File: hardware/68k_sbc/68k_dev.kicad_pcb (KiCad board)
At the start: 2 copper layers, 186.7 x 144.8 mm, 71 parts, among them IC1 DS1813-10+T&R, J1 640456-3, J2 Passive_Bus_ISA_16bit, J3 Conn_02x20_Odd_Even, J4 JTAG, J5 Barrel_Jack, SW1 SW_DPST_x2, U1 68000D, U10 CY7C1049D, U11 CY7C1049D, U12 CY7C1049D, U13 CY7C1049D, U14 16550, U15 TXS0108EPW, U2 M27C1024, U3 EPM7128SLC84-15N, U5 AMS1117-3.3, U6 CY7C1049D, U7 CY7C1049D, U8 CY7C1049D, U9 CY7C1049D, X1 CXO_DIP8, X2 CXO_DIP14

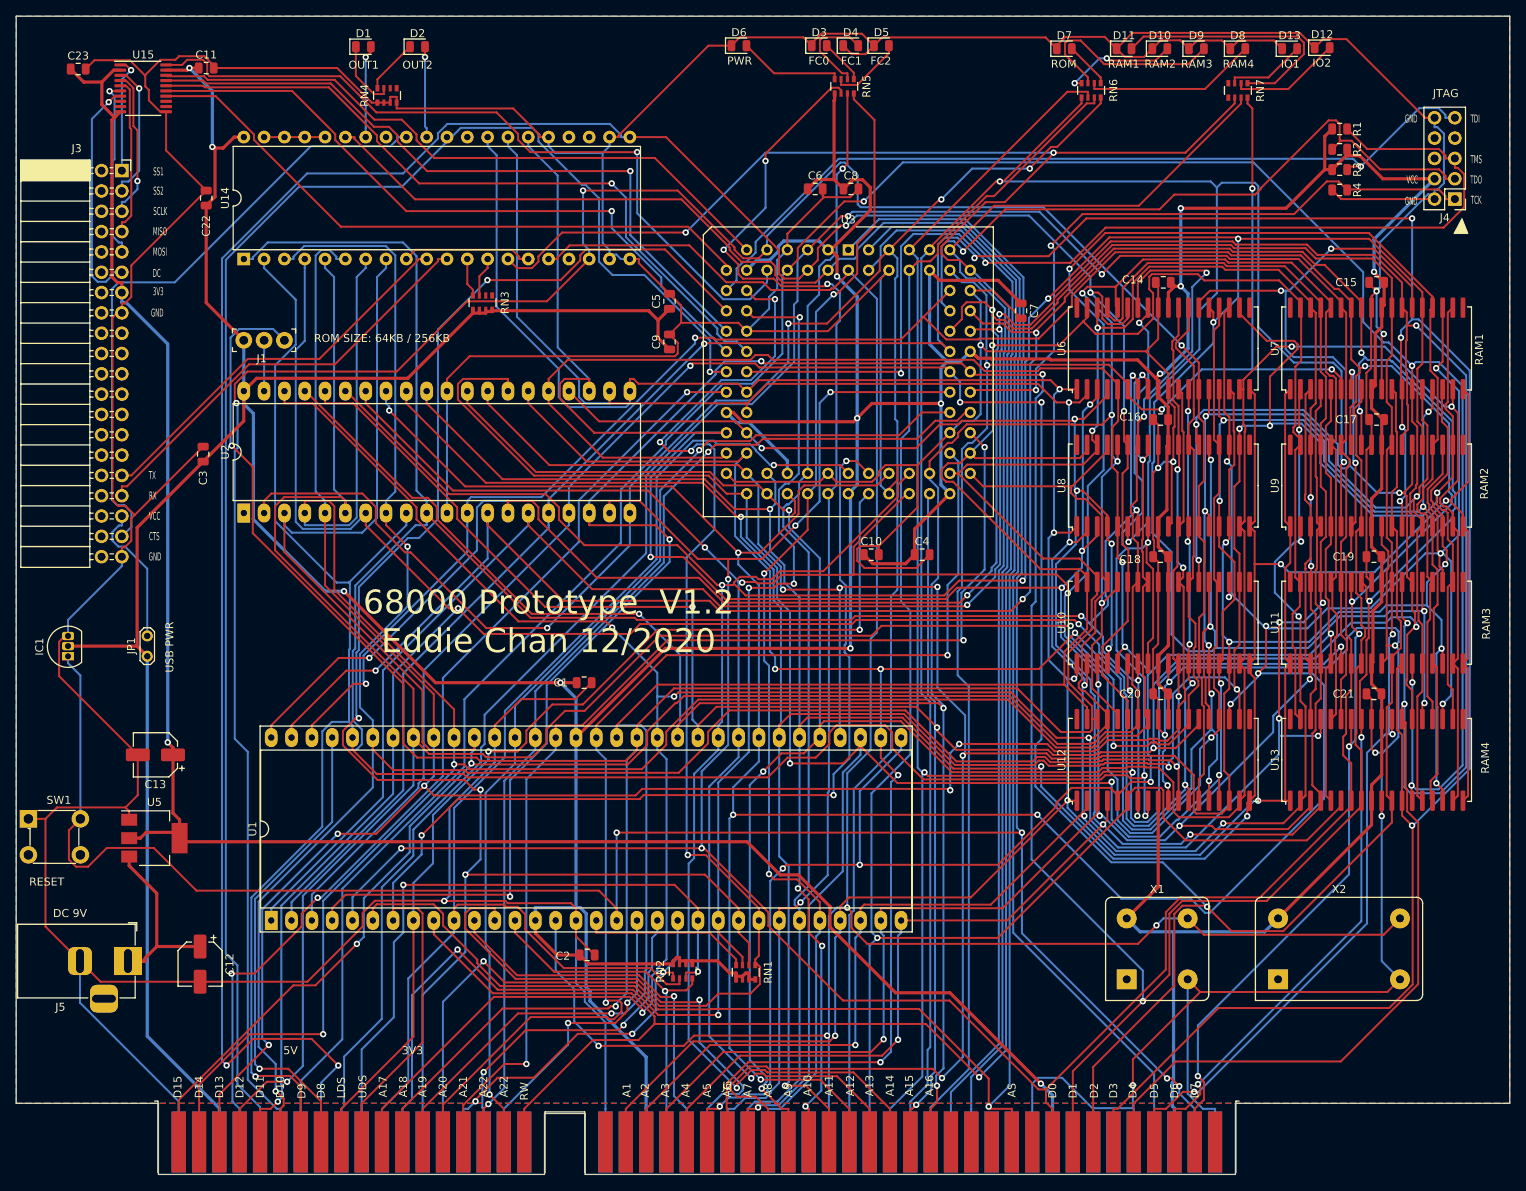
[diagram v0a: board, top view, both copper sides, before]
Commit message: Fixed v1.2 pcb design bug
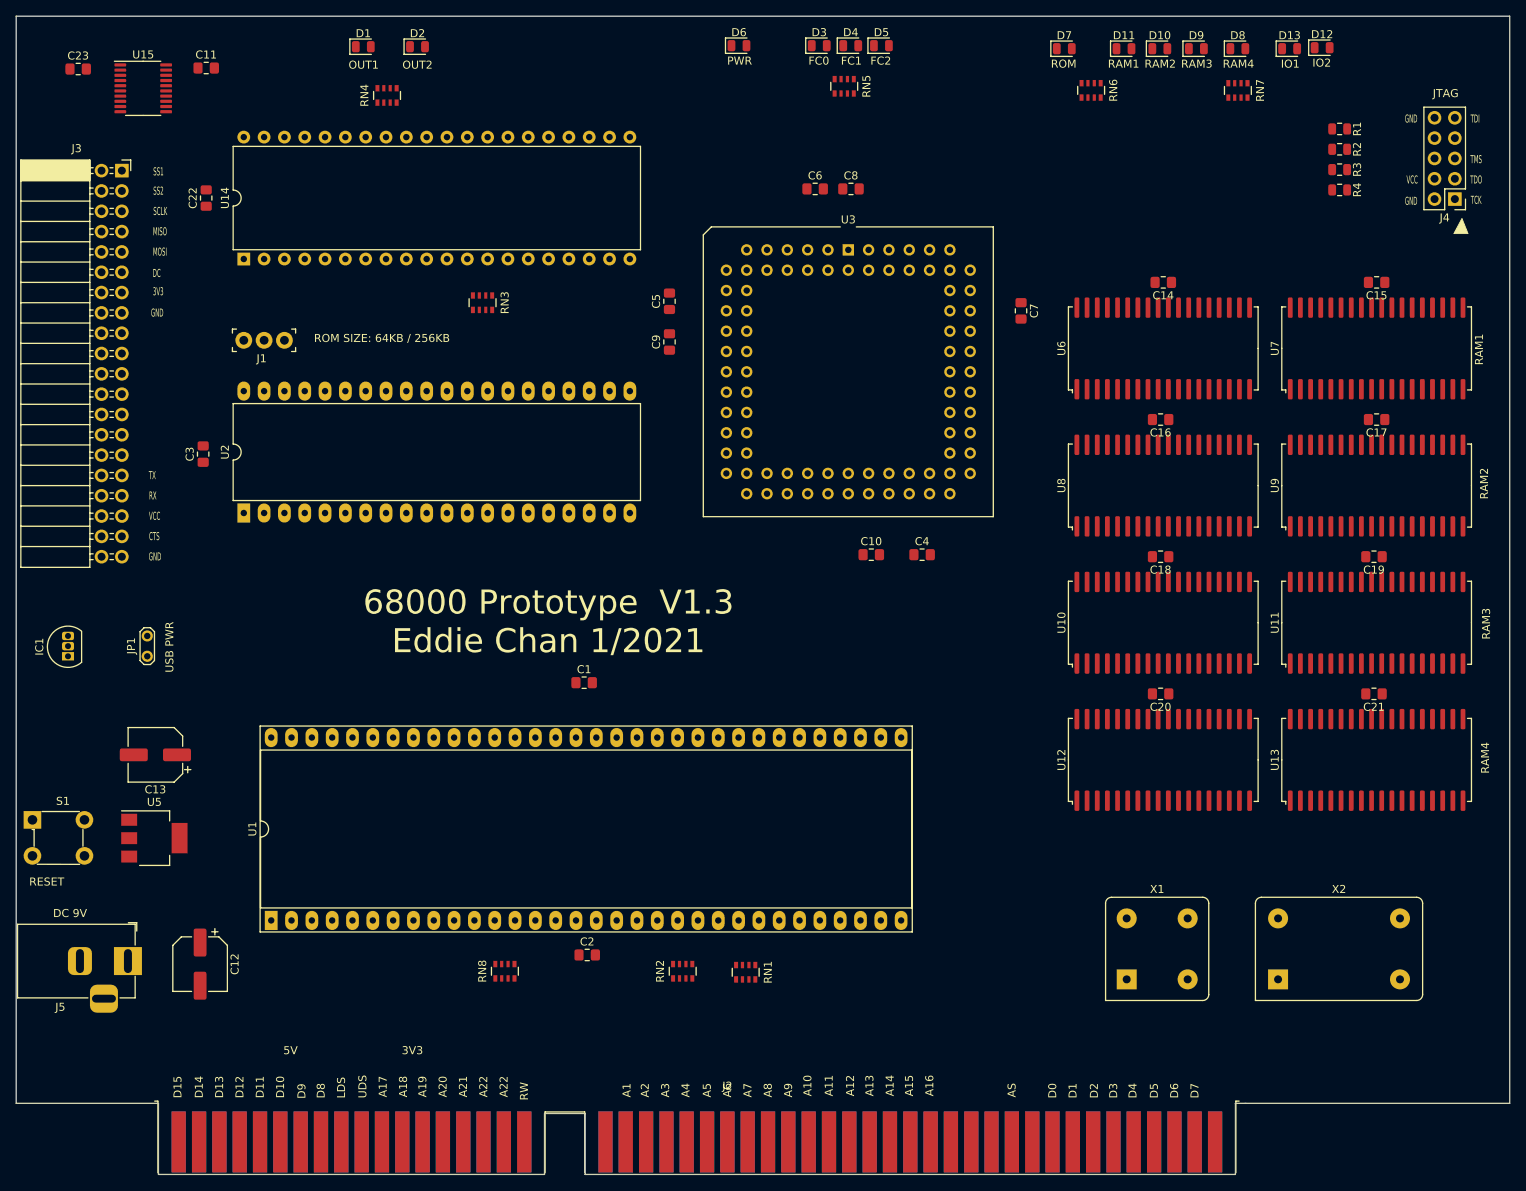
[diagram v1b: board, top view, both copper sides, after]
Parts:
- removed SW1: SW_DPST_x2, digikey-footprints:Switch_Tactile_THT_6x6mm
- added RN8: 470, Resistor_SMD:R_Array_Convex_4x0603, F.Cu at (77.6, 133.3)
- added S1: 1825910-6, digikey-footprints:Switch_Tactile_THT_6x6mm, F.Cu at (18.5, 114.4)
- C1, C10, C11, C14, C15, C16, C17, C18, C19, C2, C20, C21, C22, C23, C3, C4, C5, C6, C7, C8, C9: footprint Capacitor_SMD:C_0805_2012Metric -> Capacitor_SMD:C_0805_2012Metric_Pad1.15x1.40mm_HandSolder
- C12, C13: footprint Capacitor_SMD:CP_Elec_5x5.4 -> Capacitor_SMD:CP_Elec_6.3x7.7
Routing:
- net GND: track 1224.0 -> 0.00 mm, vias 13 -> 0
- net VCC: track 968.4 -> 0.00 mm, vias 12 -> 0
- net A14: track 481.0 -> 0.00 mm, vias 10 -> 0
- net A13: track 458.3 -> 0.00 mm, vias 6 -> 0
- net A12: track 431.2 -> 0.00 mm, vias 13 -> 0
- net A15: track 428.4 -> 0.00 mm, vias 10 -> 0
- net D4: track 422.5 -> 0.00 mm, vias 6 -> 0
- net A17: track 410.1 -> 0.00 mm, vias 8 -> 0
- net A18: track 404.0 -> 0.00 mm, vias 6 -> 0
- net D3: track 400.2 -> 0.00 mm, vias 7 -> 0
- net A3: track 382.8 -> 0.00 mm, vias 9 -> 0
- net A16: track 376.5 -> 0.00 mm, vias 7 -> 0
- net A8: track 372.5 -> 0.00 mm, vias 10 -> 0
- net A6: track 367.6 -> 0.00 mm, vias 11 -> 0
- net A11: track 363.1 -> 0.00 mm, vias 7 -> 0
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- removed copper zone on B.Cu, net GND
- removed copper zone on F.Cu, net GND
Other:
- board text added: "68000 Prototype V1.3 Eddie Chan 1/2021"
- board text removed: "68000 Prototype V1.2 Eddie Chan 12/2020"

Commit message: lib refactor
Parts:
- removed D10, D11, D12, D13, D8, D9: LED, LED_SMD:LED_0805_2012Metric
- removed RN6, RN7: 470, Resistor_SMD:R_Array_Convex_4x0603
- added C24: 100nF, Capacitor_SMD:C_0805_2012Metric_Pad1.15x1.40mm_HandSolder, B.Cu at (153.5, 72.8)
- added C25: 100nF, Capacitor_SMD:C_0805_2012Metric_Pad1.15x1.40mm_HandSolder, B.Cu at (153.5, 89.9)
- added C26: 100nF, Capacitor_SMD:C_0805_2012Metric_Pad1.15x1.40mm_HandSolder, B.Cu at (153.7, 55.1)
- added C27: 100nF, Capacitor_SMD:C_0805_2012Metric_Pad1.15x1.40mm_HandSolder, B.Cu at (181.5, 72.4)
- added U16: CY7C1049D, KiCad_Libraries:SOJ-36_10.16x23.49mm_P1.27mm_sram, F.Cu at (153.6, 55.3)
- added U17: CY7C1049D, KiCad_Libraries:SOJ-36_10.16x23.49mm_P1.27mm_sram, F.Cu at (181.5, 72.6)
- added U18: CY7C1049D, KiCad_Libraries:SOJ-36_10.16x23.49mm_P1.27mm_sram, F.Cu at (153.5, 72.6)
- added U4: CY7C1049D, KiCad_Libraries:SOJ-36_10.16x23.49mm_P1.27mm_sram, F.Cu at (181.6, 55.3)
- C1, C10, C11, C14, C15, C16, C17, C18, C19, C2, C20, C21, C22, C23, C3, C4, C5, C6, C7, C8, C9, RN2, RN8: moved to B.Cu
- moved C3 112.6 mm to (144.7, 27.6), turned to 270 degrees
- moved U2 106.6 mm to (144.7, 38.2)
- moved J1 94.8 mm to (137.9, 19.1)
- moved U7 92.2 mm to (153.5, 141.5), turned to 270 degrees
- moved U6 88.7 mm to (181.5, 141.5), turned to 270 degrees
- moved C16 77.7 mm to (153.5, 141.9), turned to 0 degrees
- moved C17 77.1 mm to (181.5, 141.4), turned to 0 degrees
- moved J4 74.5 mm to (124.0, 19.2), turned to 270 degrees
- moved D7 74.5 mm to (73.0, 18.7)
- moved R1 66.9 mm to (115.1, 29.8), turned to 90 degrees
- moved R2 64.3 mm to (117.6, 29.8), turned to 270 degrees
- moved R3 61.9 mm to (120.1, 29.8), turned to 90 degrees
- moved U9 61.3 mm to (153.5, 124.3), turned to 270 degrees
- moved X2 60.1 mm to (114.7, 142.6)
- moved R4 59.6 mm to (122.7, 29.8), turned to 270 degrees
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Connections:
- D7 pad 1: GND -> Net-(D7-Pad1)
- D7 pad 2: Net-(D7-Pad2) -> VCC
- J2 pad 13: IO_SEL1 -> Net-(J2-Pad13)
- J2 pad 14: IO_SEL2 -> Net-(J2-Pad14)
- J2 pad 15: RAM1_SEL -> Net-(J2-Pad15)
- J2 pad 16: RAM2_SEL -> Net-(J2-Pad16)
- J2 pad 17: RAM3_SEL -> Net-(J2-Pad17)
- J2 pad 18: RAM4_SEL -> Net-(J2-Pad18)
- J2 pad 19: ROM_SEL -> Net-(J2-Pad19)
- J2 pad 4: RST_H -> Net-(J2-Pad4)
- J2 pad 72: RDL -> Net-(J2-Pad72)
- J2 pad 73: RDU -> Net-(J2-Pad73)
- J2 pad 74: WRL -> Net-(J2-Pad74)
- J2 pad 75: WRU -> Net-(J2-Pad75)
- J2 pad 76: IRQ1 -> Net-(J2-Pad76)
- J2 pad 77: IRQ2 -> Net-(J2-Pad77)
- J2 pad 9: +3V3 -> Net-(J2-Pad9)
- RN1 pad 1: IPL0 -> IPL2
- RN1 pad 3: IPL2 -> IPL0
- RN2 pad 2: DTACK -> Net-(RN2-Pad2)
- RN2 pad 4: BR -> VMA
- RN4 pad 5: Net-(RN4-Pad5) -> Net-(D7-Pad1)
- RN4 pad 7: Net-(D1-Pad1) -> Net-(D2-Pad1)
- RN4 pad 8: Net-(D2-Pad1) -> Net-(D1-Pad1)
- RN5 pad 1: Net-(D3-Pad2) -> Net-(D5-Pad2)
- RN5 pad 3: Net-(D5-Pad2) -> Net-(D3-Pad2)
- RN5 pad 5: VCC -> STATUS
- RN5 pad 6: FC2 -> FC0
- RN5 pad 8: FC0 -> FC2
- RN8 pad 1: BGACK -> Net-(RN8-Pad1)
- RN8 pad 2: VMA -> BR
- RN8 pad 3: Net-(RN8-Pad3) -> BGACK
- RN8 pad 4: Net-(RN8-Pad4) -> DTACK
- U1 pad 17: Net-(RN1-Pad4) -> Net-(RN8-Pad1)
- U14 pad 30: IRQ1 -> Net-(U14-Pad30)
- U3 pad 22: IRQ1 -> IO_SEL1
- U3 pad 24: IRQ2 -> STATUS
- U3 pad 74: IO_SEL1 -> RAM5_SEL
- U3 pad 75: IO_SEL2 -> RAM6_SEL
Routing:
- net GND: track 0.00 -> 1228.2 mm, vias 0 -> 19
- net VCC: track 0.00 -> 1070.5 mm, vias 0 -> 25
- net A3: track 0.00 -> 593.9 mm, vias 0 -> 11
- net A17: track 0.00 -> 536.0 mm, vias 0 -> 8
- net A1: track 0.00 -> 525.3 mm, vias 0 -> 5
- net A16: track 0.00 -> 472.6 mm, vias 0 -> 9
- net A7: track 0.00 -> 471.9 mm, vias 0 -> 8
- net A2: track 0.00 -> 469.3 mm, vias 0 -> 10
- net A5: track 0.00 -> 464.2 mm, vias 0 -> 10
- net A9: track 0.00 -> 449.3 mm, vias 0 -> 5
- net A4: track 0.00 -> 447.2 mm, vias 0 -> 8
- net A8: track 0.00 -> 446.9 mm, vias 0 -> 10
- net A6: track 0.00 -> 445.8 mm, vias 0 -> 11
- net A18: track 0.00 -> 443.0 mm, vias 0 -> 6
- net A11: track 0.00 -> 426.3 mm, vias 0 -> 8
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- added copper zone on B.Cu, net GND
- added copper zone on F.Cu, net GND
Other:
- board size 186.7 x 144.8 mm -> 186.7 x 155.4 mm
- board text added: "RAM5"
- board text added: "RAM6"
- board text added: "STATUS"
- board text removed: "IO1"
- board text removed: "IO1_SEL"
- board text removed: "IO2"
- board text removed: "IO2_SEL"
- board text removed: "RAM1_SEL"
- board text removed: "RAM2_SEL"
- board text removed: "RAM3_SEL"
- board text removed: "RAM4_SEL"
- board text removed: "ROM"
- board text removed: "ROM_SEL"

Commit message: updates
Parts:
- removed C11: 100nF, Capacitor_SMD:C_0805_2012Metric_Pad1.15x1.40mm_HandSolder
- removed X1: CXO_DIP8, Oscillator:Oscillator_DIP-8_LargePads
- added C28: 100nF, Capacitor_SMD:C_0805_2012Metric_Pad1.15x1.40mm_HandSolder, B.Cu at (227.3, 146.9)
- added C29: 100nF, Capacitor_SMD:C_0805_2012Metric_Pad1.15x1.40mm_HandSolder, B.Cu at (126.0, 129.4)
- added C30: 100nF, Capacitor_SMD:C_0805_2012Metric_Pad1.15x1.40mm_HandSolder, B.Cu at (160.0, 123.4)
- added C31: 100nF, Capacitor_SMD:C_0805_2012Metric_Pad1.15x1.40mm_HandSolder, B.Cu at (196.3, 124.0)
- added C32: 100nF, Capacitor_SMD:C_0805_2012Metric_Pad1.15x1.40mm_HandSolder, F.Cu at (138.7, 123.6)
- added C33: 100nF, Capacitor_SMD:C_0805_2012Metric_Pad1.15x1.40mm_HandSolder, B.Cu at (113.0, 13.8)
- added C34: 100nF, Capacitor_SMD:C_0805_2012Metric_Pad1.15x1.40mm_HandSolder, B.Cu at (100.8, 13.8)
- added G***: LOGO, logos:twitter, F.Cu at (139.3, 132.8)
- added U20: 74LS244, Package_SO:SSOP-20_5.3x7.2mm_P0.65mm, F.Cu at (180.2, 128.8)
- added U21: 74LS244, Package_SO:SSOP-20_5.3x7.2mm_P0.65mm, B.Cu at (138.7, 128.7)
- added U22: 74LS244, Package_SO:SSOP-20_5.3x7.2mm_P0.65mm, F.Cu at (196.3, 128.9)
- added U23: SN74LVC245AN, KiCad_Libraries:SOIC127P1032X265-20N, F.Cu at (219.5, 147.1)
- added U24: SN74LVC245AN, KiCad_Libraries:SOIC127P1032X265-20N, F.Cu at (118.0, 129.3)
- added U25: TXS0108EPW, Package_SO:TSSOP-20_4.4x6.5mm_P0.65mm, F.Cu at (106.9, 18.3)
- RN1, RN3: moved to B.Cu
- U15: value TXS0108EPW -> 74LS244; footprint Package_SO:TSSOP-20_4.4x6.5mm_P0.65mm -> Package_SO:SSOP-20_5.3x7.2mm_P0.65mm
- moved C23 168.4 mm to (180.2, 123.8), turned to 180 degrees
- moved U15 159.7 mm to (160.1, 128.7)
- moved X2 119.4 mm to (191.5, 51.2), turned to 270 degrees
- moved RN4 72.9 mm to (142.6, 20.1)
- moved C22 72.6 mm to (121.9, 69.3)
- moved U14 72.6 mm to (133.1, 70.7)
- moved C14 70.1 mm to (251.1, 44.5), turned to 0 degrees
- moved C15 70.1 mm to (250.7, 78.7)
- moved C16 70.1 mm to (222.7, 130.9)
- moved C17 70.1 mm to (250.7, 130.4)
- moved C18 70.1 mm to (222.9, 113.3)
- moved C19 70.1 mm to (250.7, 113.3)
- moved C20 70.1 mm to (222.8, 96.3)
- moved C24 70.1 mm to (222.8, 61.8)
- moved C25 70.1 mm to (222.8, 79.0)
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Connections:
- C23 pad 1: +3V3 -> VCC
- J2 pad 20: CPU_CLK -> BUS_CPU_CLK
- J2 pad 23: FC0 -> BUS_FC0
- J2 pad 24: FC1 -> BUS_FC1
- J2 pad 25: FC2 -> BUS_FC2
- J2 pad 27: BG -> BUS_BG
- J2 pad 33: D7 -> BUS_D7
- J2 pad 34: D6 -> BUS_D6
- J2 pad 35: D5 -> BUS_D5
- J2 pad 36: D4 -> BUS_D4
- J2 pad 37: D3 -> BUS_D3
- J2 pad 38: D2 -> BUS_D2
- J2 pad 39: D1 -> BUS_D1
- J2 pad 40: D0 -> BUS_D0
- J2 pad 42: AS -> BUS_AS
- J2 pad 46: A16 -> BUS_A16
- J2 pad 47: A15 -> BUS_A15
- J2 pad 48: A14 -> BUS_A14
- J2 pad 49: A13 -> BUS_A13
- J2 pad 50: A12 -> BUS_A12
- J2 pad 51: A11 -> BUS_A11
- J2 pad 52: A10 -> BUS_A10
- J2 pad 53: A9 -> BUS_A9
- J2 pad 54: A8 -> BUS_A8
- J2 pad 55: A7 -> BUS_A7
- J2 pad 56: A6 -> BUS_A6
- J2 pad 57: A5 -> BUS_A5
- J2 pad 58: A4 -> BUS_A4
- J2 pad 59: A3 -> BUS_A3
- J2 pad 60: A2 -> BUS_A2
- J2 pad 61: A1 -> BUS_A1
- J2 pad 81: RW -> BUS_RW
- J2 pad 82: A23 -> BUS_A23
- J2 pad 83: A22 -> BUS_A22
- J2 pad 84: A21 -> BUS_A21
- J2 pad 85: A20 -> BUS_A20
- J2 pad 86: A19 -> BUS_A19
- J2 pad 87: A18 -> BUS_A18
- J2 pad 88: A17 -> BUS_A17
- J2 pad 89: UDS -> BUS_UDS
- J2 pad 90: LDS -> BUS_LDS
- J2 pad 91: D8 -> BUS_D8
- J2 pad 92: D9 -> BUS_D9
- J2 pad 93: D10 -> BUS_D10
- J2 pad 94: D11 -> BUS_D11
- J2 pad 95: D12 -> BUS_D12
- J2 pad 96: D13 -> BUS_D13
- J2 pad 97: D14 -> BUS_D14
- J2 pad 98: D15 -> BUS_D15
- U15 pad 1: Net-(J3-Pad1) -> GND
- U15 pad 10: +3V3 -> GND
- U15 pad 11: GND -> A20
- U15 pad 12: Net-(U15-Pad12) -> BUS_A21
- U15 pad 13: Net-(U15-Pad13) -> A19
- U15 pad 14: DC -> BUS_A22
- U15 pad 15: MOSI -> A18
- U15 pad 16: MISO -> BUS_A23
- U15 pad 17: SCLK -> A17
- U15 pad 18: SS2 -> BUS_RW
- U15 pad 19: VCC -> GND
- U15 pad 2: +3V3 -> RW
- U15 pad 20: SS1 -> VCC
- U15 pad 3: Net-(J3-Pad3) -> BUS_A17
- U15 pad 4: Net-(J3-Pad5) -> A23
- U15 pad 5: Net-(J3-Pad7) -> BUS_A18
- U15 pad 6: Net-(J3-Pad9) -> A22
- U15 pad 7: Net-(J3-Pad11) -> BUS_A19
- U15 pad 8: Net-(U15-Pad8) -> A21
- U15 pad 9: Net-(U15-Pad9) -> BUS_A20
- U3 pad 31: A6 -> A18
- U3 pad 33: A7 -> A19
- U3 pad 34: A8 -> A20
- U3 pad 35: A9 -> A21
- U3 pad 36: A10 -> A22
- U3 pad 37: A11 -> A23
- U3 pad 48: A12 -> IPL2
- U3 pad 49: A13 -> IPL1
- U3 pad 50: A14 -> IPL0
- U3 pad 51: A15 -> BUS_DIR_CTRL
- U3 pad 52: A16 -> D0
- U3 pad 54: A17 -> D1
- U3 pad 55: A18 -> D2
- U3 pad 56: A19 -> D3
- U3 pad 57: A20 -> D4
- U3 pad 58: A21 -> D5
- U3 pad 60: A22 -> D6
- U3 pad 61: A23 -> D7
- U3 pad 63: D0 -> D8
- U3 pad 64: D1 -> D9
- U3 pad 65: D2 -> D10
- U3 pad 67: D3 -> D11
- U3 pad 68: D4 -> D12
- U3 pad 69: D5 -> D13
- U3 pad 70: D6 -> D14
- U3 pad 73: D7 -> D15
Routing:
- net GND: track 1228.2 -> 1460.2 mm, vias 19 -> 28
- net BUS_DIR_CTRL: track 0.00 -> 206.3 mm, vias 0 -> 1
- net RAM4_SEL: track 105.7 -> 242.0 mm, vias 3 -> 5
- net A8: track 446.9 -> 316.0 mm, vias 10 -> 3
- net A7: track 471.9 -> 357.6 mm, vias 8 -> 9
- net BUS_CPU_CLK: track 0.00 -> 110.4 mm, vias 0 -> 2
- net A10: track 422.9 -> 320.7 mm, vias 1 -> 2
- net A9: track 449.3 -> 349.5 mm, vias 5 -> 7
- net A17: track 536.0 -> 446.9 mm, vias 8 -> 6
- net A6: track 445.8 -> 362.1 mm, vias 11 -> 6
- net A1: track 525.3 -> 441.8 mm, vias 5 -> 4
- net RW: track 143.4 -> 225.8 mm, vias 3 -> 5
- net AS: track 198.7 -> 117.3 mm, vias 3 -> 5
- net BUS_AS: track 0.00 -> 80.7 mm, vias 0 -> 3
- net D13: track 408.7 -> 330.7 mm, vias 4 -> 7
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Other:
- board size 186.7 x 155.4 mm -> 190.5 x 158.4 mm
- board text added: "68000 Prototype V1.4 Eddie Chan 02/2021"
- board text removed: "68000 Prototype V1.3 Eddie Chan 1/2021"
